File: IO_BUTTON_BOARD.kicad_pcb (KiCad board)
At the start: 2 copper layers, 80 x 40 mm, 139 parts, among them P1 I2C, P10 IO_7, P2 I2C, P3 IO_0, P4 IO_1, P5 IO_2, P6 IO_3, P7 IO_4, P8 IO_5, P9 IO_6, Q1 NPN, Q10 PNP, Q11 PNP, Q12 PNP, Q13 PNP, Q14 PNP, Q15 PNP, Q16 PNP, Q17 PNP, Q2 PNP, Q3 NPN, Q4 PNP, Q5 NPN, Q6 NPN, Q7 PNP, Q8 PNP, Q9 NPN, SW1 CONFIG, SW10 SW_Push, SW11 SW_Push, SW12 SW_Push, SW13 SW_Push, SW14 SW_Push, SW15 SW_Push, SW16 SW_Push, SW17 SW_Push, SW2 SW_0, SW3 SW_1, SW4 SW_2, SW5 SW_3, SW6 SW_4, SW7 SW_5, SW8 SW_6, SW9 SW_7, U1 PCF8574A, U2 74HC86, U3 74HC86

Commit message: Route completed
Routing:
- net Net-(D10-Pad2): track 9.43 -> 106.0 mm, vias 1 -> 9
- net Net-(R57-Pad1): track 4.47 -> 89.8 mm, vias 0 -> 6
- net Net-(R42-Pad1): track 1.27 -> 69.1 mm, vias 0 -> 4
- net Net-(R58-Pad1): track 4.47 -> 55.3 mm, vias 0 -> 1
- net Net-(R54-Pad1): track 14.9 -> 65.0 mm, vias 0 -> 4
- net Net-(R36-Pad1): track 1.27 -> 46.3 mm, vias 0 -> 6
- net Net-(R41-Pad1): track 1.27 -> 43.0 mm, vias 0 -> 2
- net Net-(R40-Pad1): track 1.27 -> 38.5 mm, vias 0 -> 4
- net Net-(R56-Pad1): track 4.47 -> 41.3 mm, vias 0 -> 3
- net Net-(D12-Pad2): track 9.69 -> 45.6 mm, vias 1 -> 3
- net Net-(R35-Pad1): track 1.54 -> 33.2 mm, vias 0 -> 2
- net Net-(D8-Pad2): track 9.02 -> 40.5 mm, vias 1 -> 3
- net Net-(R55-Pad1): track 4.47 -> 35.6 mm, vias 0 -> 2
- net Net-(D11-Pad2): track 9.43 -> 39.7 mm
- net Net-(R39-Pad1): track 1.27 -> 29.9 mm, vias 0 -> 2
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
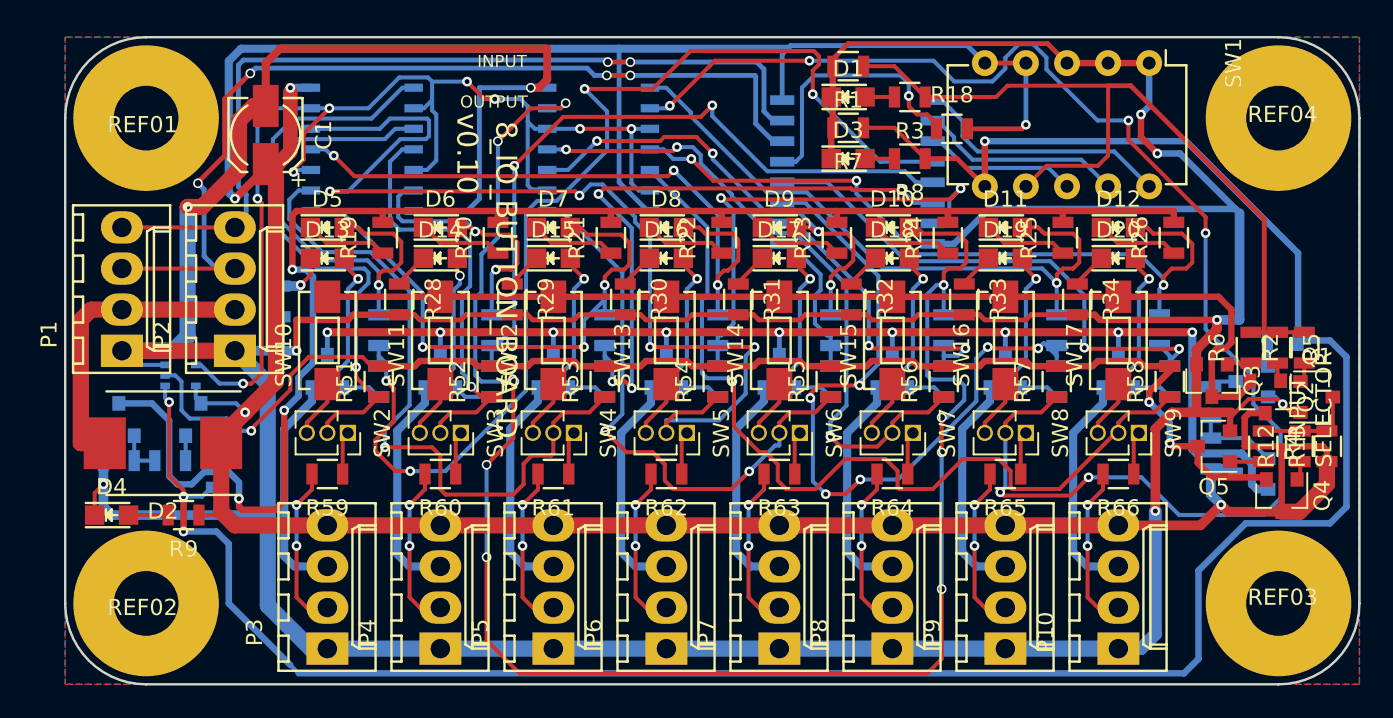
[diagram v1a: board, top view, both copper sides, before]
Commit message: Increased track width
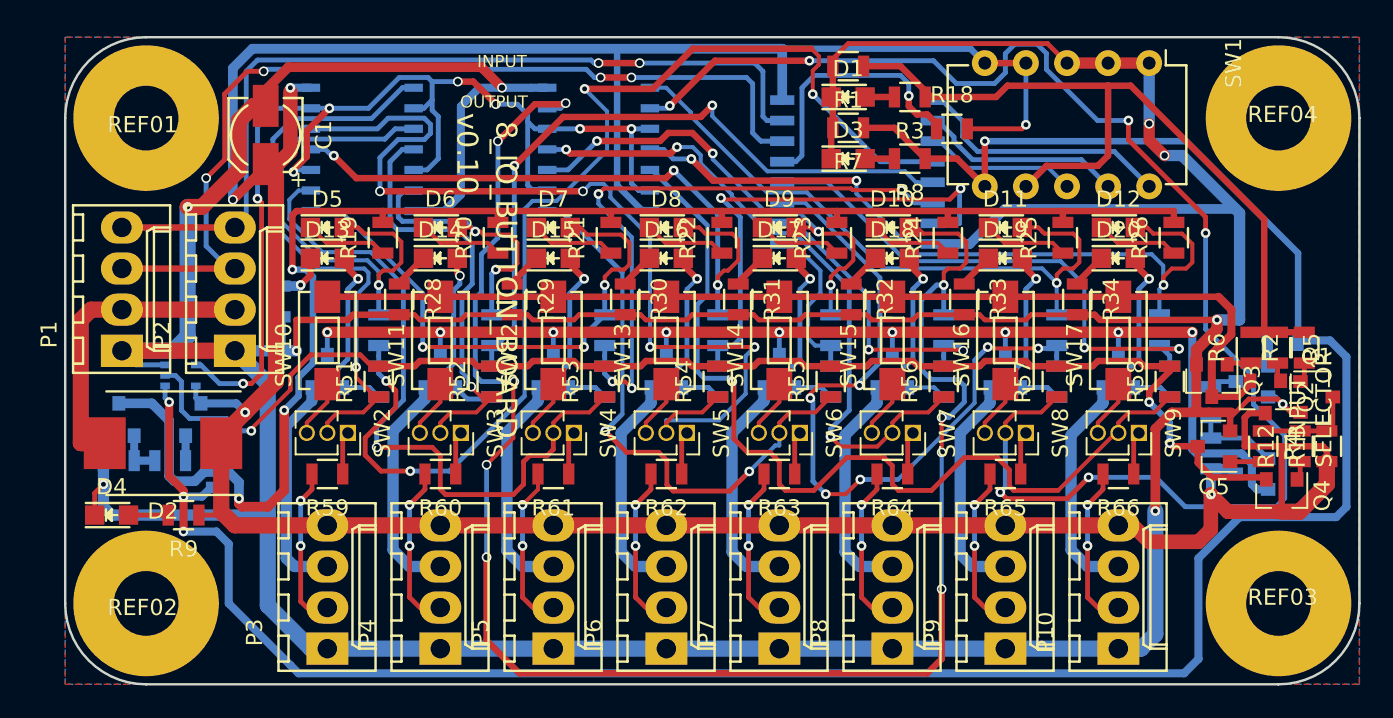
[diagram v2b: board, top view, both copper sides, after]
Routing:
- net GND: track 326.9 -> 318.6 mm
- net Net-(R54-Pad1): track 65.0 -> 59.9 mm
- net VCC: track 208.4 -> 210.0 mm
- net Net-(R38-Pad1): track 9.61 -> 11.1 mm
- net Net-(R58-Pad1): track 55.3 -> 56.7 mm
- net Net-(R39-Pad1): track 29.9 -> 31.0 mm
- net /SCL: track 59.1 -> 58.1 mm
- net /SDA: track 55.1 -> 54.1 mm
- net Net-(R42-Pad1): track 69.1 -> 70.1 mm
- net Net-(D7-Pad2): track 35.4 -> 34.4 mm
- net Net-(R35-Pad1): track 33.2 -> 34.1 mm
- net /INPUT_LED_GND: track 96.4 -> 95.6 mm
- net Net-(R57-Pad1): track 89.8 -> 90.5 mm
- net Net-(R40-Pad1): track 38.5 -> 37.8 mm

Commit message: Edit silkscreen
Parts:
- renumbered SW1 to CONF, P1 to I2C, P2 to I2C, SW2 to IO_0, D5 to IO_0, SW3 to IO_1, D6 to IO_1, SW4 to IO_2, D7 to IO_2, SW5 to IO_3, D8 to IO_3, SW6 to IO_4, D9 to IO_4, SW7 to IO_5, D10 to IO_5, SW8 to IO_6, D11 to IO_6, SW9 to IO_7, D12 to IO_7, D3 to OUTPUT_ON, D4 to POWER, D1 to REVERSE_ON
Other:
- board text added: "8_IO_BUTTON_BOARD - v0.10"
- board text added: "BUTTON AS INPUT"
- board text added: "Mathias DELAHAYE - 2019"
- board text added: "Mathias DELAHAYE -2019"
- board text added: "Mathias DELAHAYE 2019"
- board text added: "SENSOR AS INPUT"
- board text added: "Vin = +5V Pin {1,2,3} -> Addr I2C Pin 4 -> Reverse Pin 5 -> Ouput"
- board text removed: "INPUT SELECTOR"
- board text removed: "v0.10"
